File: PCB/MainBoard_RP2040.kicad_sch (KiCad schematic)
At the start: 23 parts, among them J1 USB4105-GF-A, U20 ATmega32U4-A, U37 Pico, Y2 Crystal_GND24

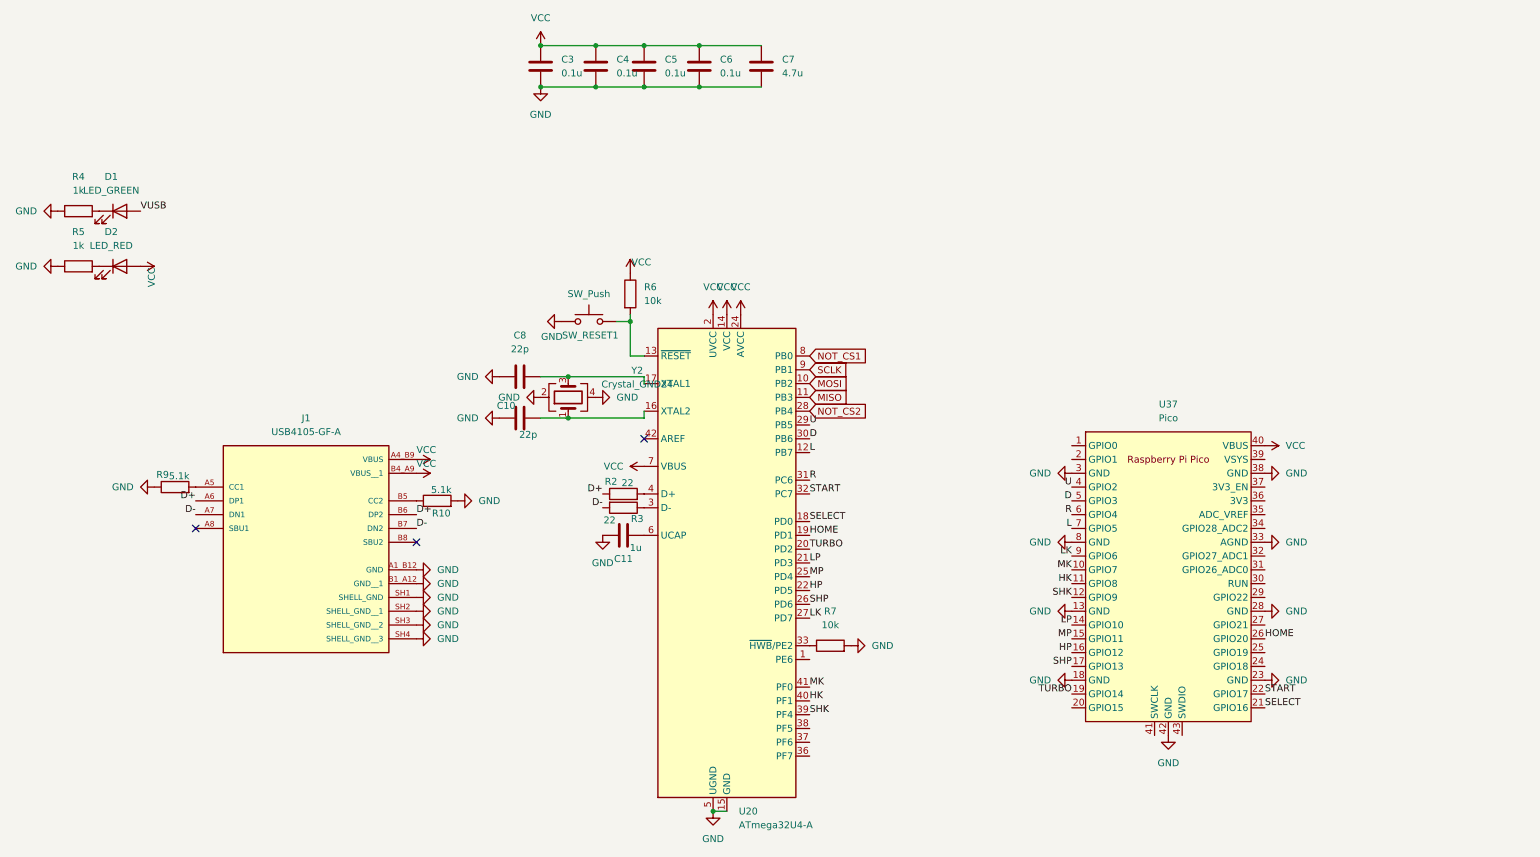
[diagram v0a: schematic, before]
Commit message: Confirmed working, moving towards PCB v1.1
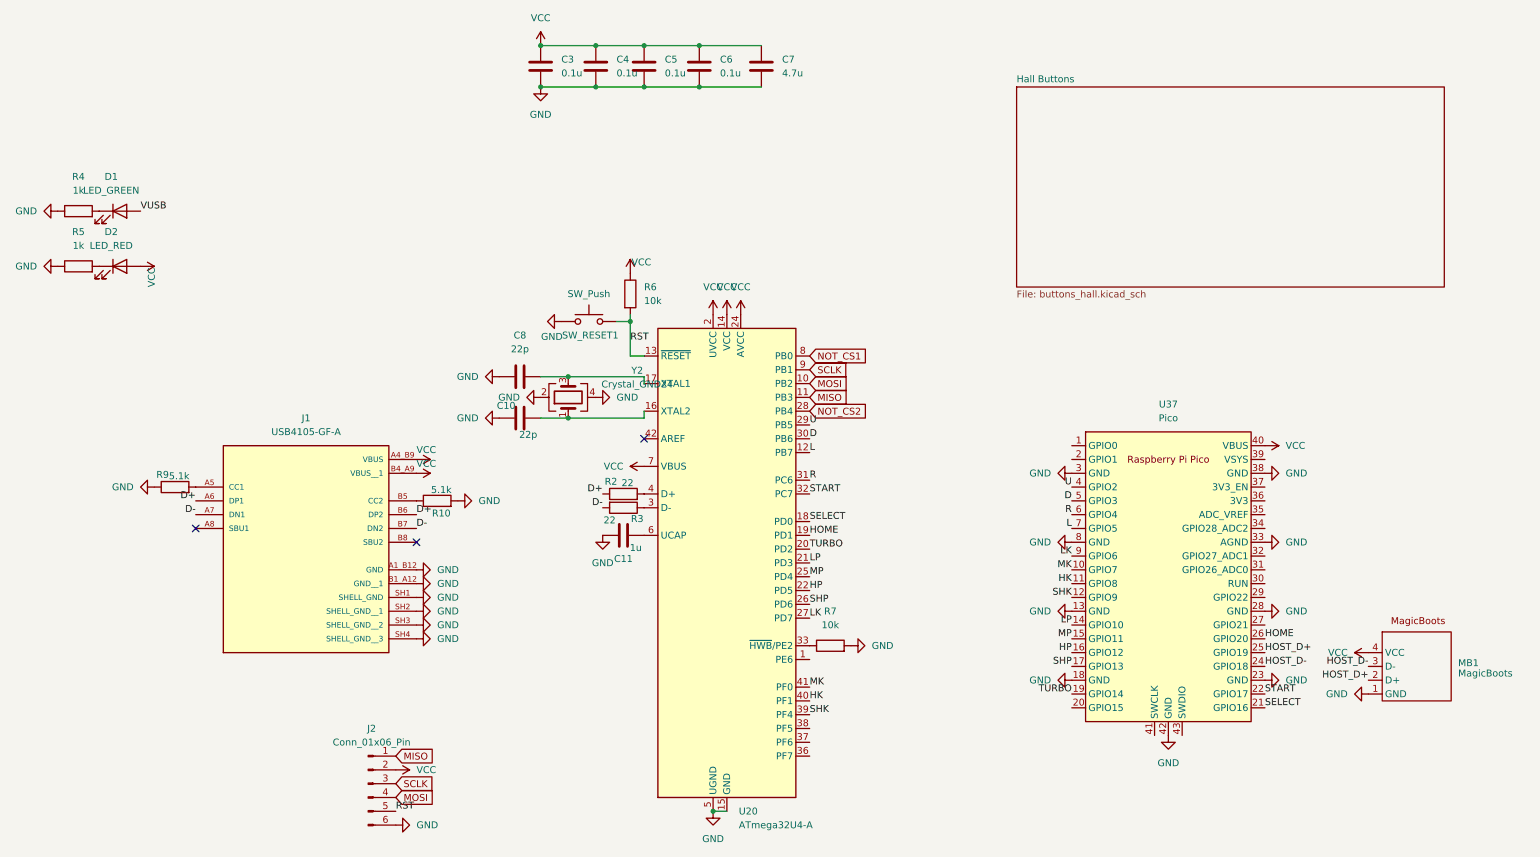
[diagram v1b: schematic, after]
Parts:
- added J2: Conn_01x06_Pin, Connector_PinHeader_2.54mm:PinHeader_2x03_P2.54mm_Vertical, symbol Connector:Conn_01x06_Pin
- added MB1: MagicBoots, Mayflash:MagicBoots, symbol HostPort_PS4:MayFlash_MagicBoots
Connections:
- net GND: now also J2.6 (Pin_6), MB1.1 (GND)
- net MISO: now also J2.1 (Pin_1)
- net MOSI: now also J2.4 (Pin_4)
- net SCLK: now also J2.3 (Pin_3)
- net VCC: now also J2.2 (Pin_2), MB1.4 (VCC)
- net RST: now reaches R6.2, SW_RESET1.2, U20.13 (~{RESET})
- net RST: now also J2.5 (Pin_5)
- net HOST_D-: now reaches U37.24 (GPIO18)
- net HOST_D-: now also MB1.3 (D-)
- net HOST_D+: now reaches U37.25 (GPIO19)
- net HOST_D+: now also MB1.2 (D+)
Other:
- added sheet Hall Buttons (buttons_hall.kicad_sch)

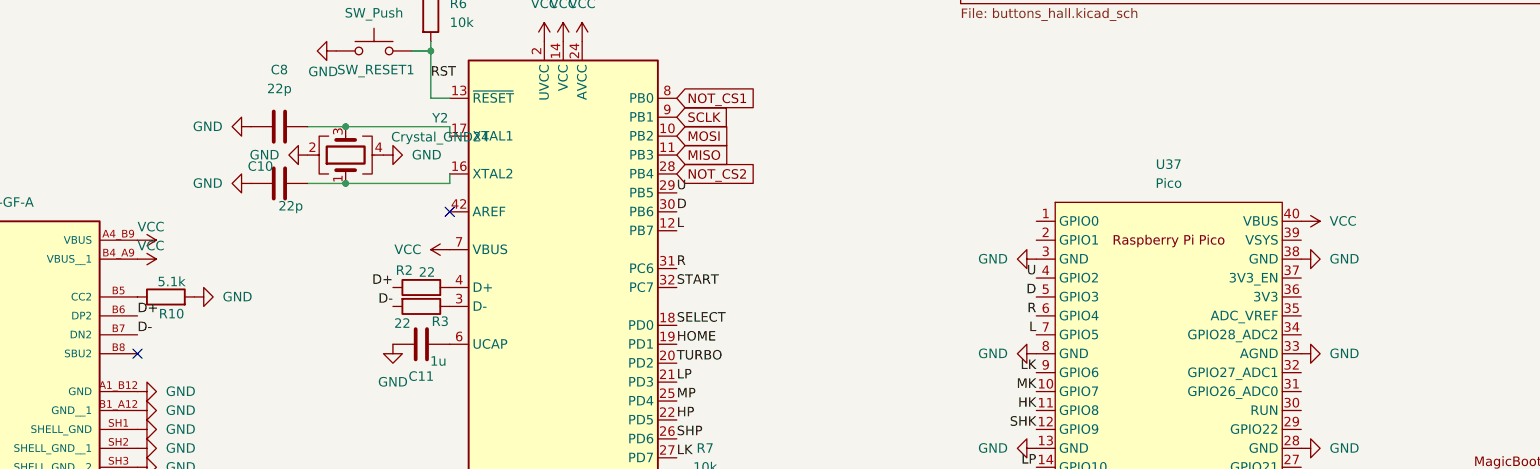
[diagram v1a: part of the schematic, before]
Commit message: Added protective diodes to RP2040 Board
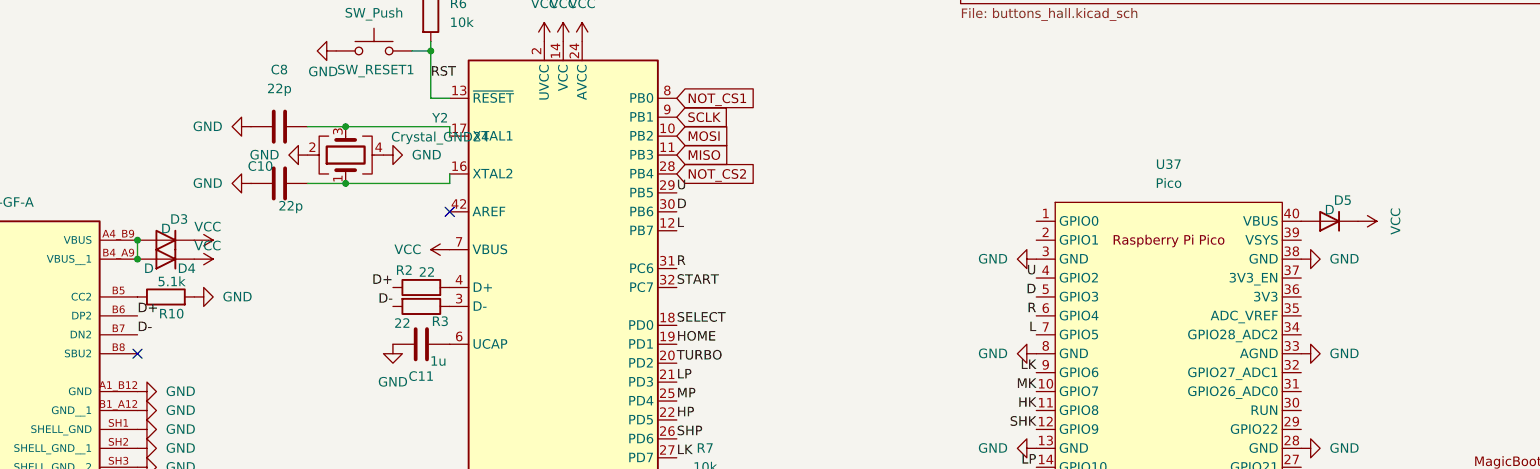
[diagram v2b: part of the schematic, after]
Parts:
- added D3, D4, D5: D, Diode_SMD:D_0603_1608Metric, symbol Device:D
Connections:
- net VCC: now also D3.1 (K), D4.1 (K), D5.1 (K); no longer J1.A4_B9 (VBUS), J1.B4_A9 (VBUS__1), U37.40 (VBUS)
- new net: D3.2 (A), D4.2 (A), J1.A4_B9 (VBUS), J1.B4_A9 (VBUS__1)
- new net: D5.2 (A), U37.40 (VBUS)
